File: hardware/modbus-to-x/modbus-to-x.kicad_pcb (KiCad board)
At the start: 4 copper layers, 55 x 55 mm, 64 parts, among them J1 PWR, J2 UART, J3 Screw_Terminal_3.5mm_2, J4 SSQ-110-X-X-D, SW1 1825910-7, SW2 1825910-7, U1 AMS1117-3.3, U2 ESP32-WROOM-32DM113DH6400PH3Q0, U3 MAX3485, U5 AT24CS64-XHM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

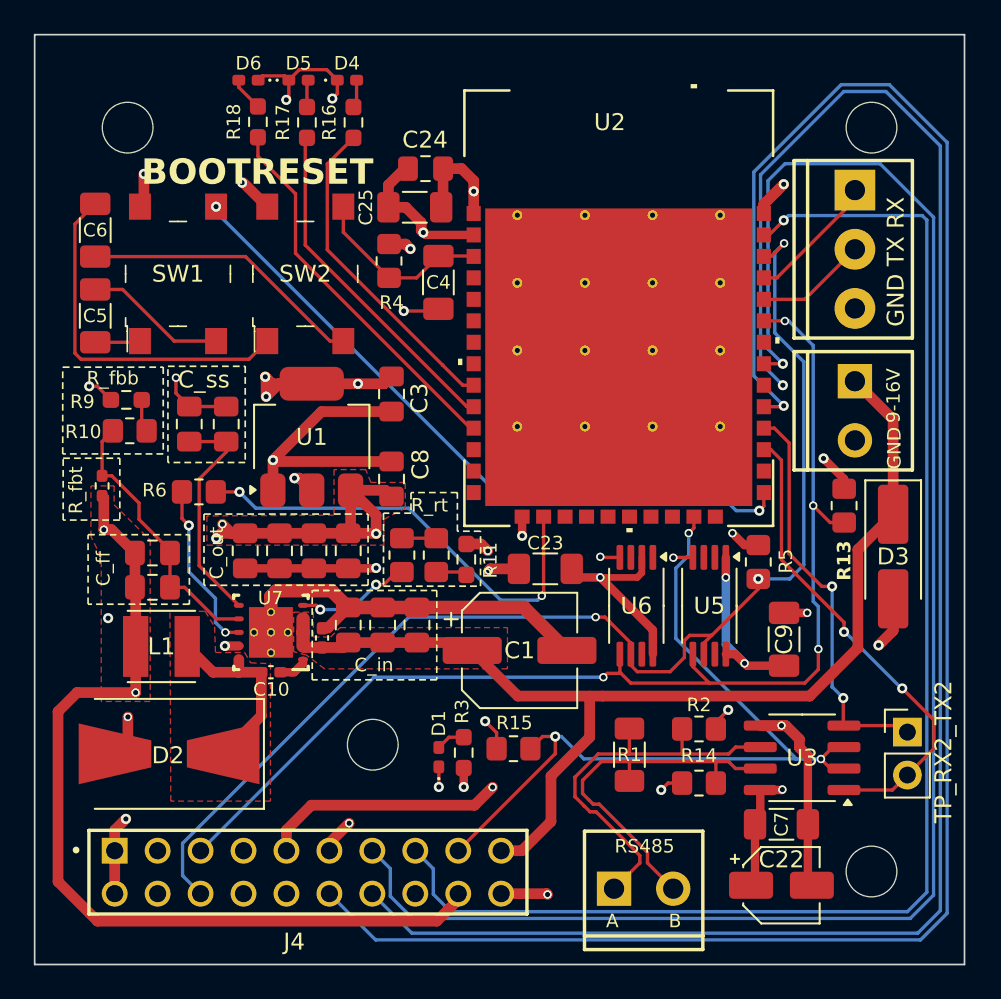
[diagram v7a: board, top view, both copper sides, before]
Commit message: improved trace clearance
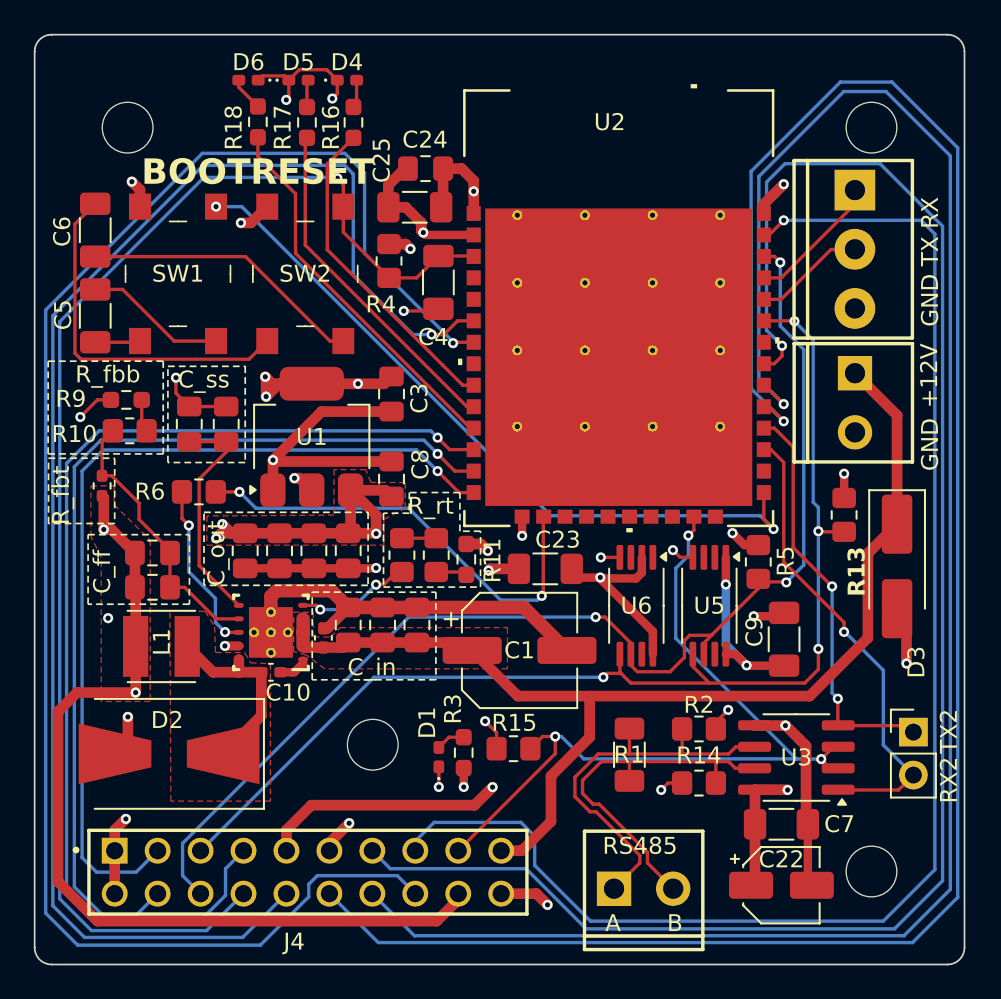
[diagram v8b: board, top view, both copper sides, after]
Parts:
- G***: footprint Modbus To X Graphics:logo -> Modbus To X Graphics:modbus_to_x_logo.kicad_40x40mm_mod
- moved G*** 13.1 mm to (116.7, 119.0)
- moved D3 0.63 mm to (131.0, 111.5)
- moved R13 0.55 mm to (127.9, 108.4)
- moved J1 0.47 mm to (128.5, 100.0)
- moved TP_RX2_TX2 0.36 mm to (132.0, 121.3)
- moved U3 0.34 mm to (125.1, 122.8)
- moved C19 0.08 mm to (97.1, 115.7)
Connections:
- J4 pad 03: unconnected-(J4-Pad03) -> /GPIO12
- J4 pad 04: unconnected-(J4-Pad04) -> /GPIO14
- J4 pad 07: unconnected-(J4-Pad07) -> /GPIO27
- J4 pad 08: unconnected-(J4-Pad08) -> /EN
- J4 pad 10: unconnected-(J4-Pad10) -> /GPIO_34
- J4 pad 16: unconnected-(J4-Pad16) -> /GPIO_35
- U2 pad 12: unconnected-(U2-IO27-Pad12) -> /GPIO27
- U2 pad 13: unconnected-(U2-IO14-Pad13) -> /GPIO14
- U2 pad 14: unconnected-(U2-IO12-Pad14) -> /GPIO12
- U2 pad 6: unconnected-(U2-IO34-Pad6) -> /GPIO_34
- U2 pad 7: unconnected-(U2-IO35-Pad7) -> /GPIO_35
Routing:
- net /GPIO_35: track 0.00 -> 97.6 mm, vias 0 -> 1
- net /GPIO_34: track 0.00 -> 87.1 mm, vias 0 -> 1
- net /EN: track 10.9 -> 79.4 mm, vias 0 -> 1
- net /GPIO27: track 0.00 -> 64.6 mm, vias 0 -> 1
- net /GPIO14: track 0.00 -> 56.0 mm, vias 0 -> 1
- net /GPIO12: track 0.00 -> 52.9 mm, vias 0 -> 1
- net /SPI_CLK: track 107.3 -> 110.4 mm
- net /IO_0: track 41.0 -> 43.3 mm
- net /SPI_CS: track 114.7 -> 116.9 mm
- net /SPI_MOSI: track 83.1 -> 84.9 mm
- net /SCL_BUS: track 74.2 -> 72.4 mm
- net GND: track 113.8 -> 115.4 mm
- net /RS485+: track 24.4 -> 23.4 mm
- net /RS485-: track 22.9 -> 22.0 mm
- net /RS485_DE_RE: track 48.1 -> 47.5 mm
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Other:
- outline, holes or cut-outs redrawn
- board text added: "+12V"
- board text added: "RX2"
- board text added: "TX2"
- board text removed: "9-16V"
